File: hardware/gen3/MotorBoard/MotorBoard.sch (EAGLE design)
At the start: 265 parts, among them M10O1 TEST_PT, M1O2 TEST_PT, M1O3 TEST_PT, M2O1 TEST_PT, M2O2 TEST_PT, M2O3 TEST_PT, M3O1 TEST_PT, M3O2 TEST_PT, M3O3 TEST_PT, M4O1 TEST_PT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

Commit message: motorbrd: just felt like I should commit
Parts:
- added R113: 10k, SparkFun-Passives:RESISTOR0805-RES
- added S1: SWITCH-MOMENTARY-2SMD-4, SparkFun-Electromechanical:SWITCH-MOMENTARY-2SMD-4
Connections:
- new net RESET1: R113.1, S1.1
- net 3.3V: now also R113.2
- net GND: now also S1.2
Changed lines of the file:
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@@
 <?xml version="1.0" encoding="utf-8"?>
 <!DOCTYPE eagle SYSTEM "eagle.dtd">
-<eagle version="7.2.0">
+<eagle version="6.4">
 <drawing>
 <settings>
@@
 <part name="C57" library="SparkFun-Passives" deviceset="CAP" device="0805" value=".1uF"/>
 <part name="C58" library="SparkFun-Passives" deviceset="CAP" device="0805" value=".1uF"/>
+<part name="S1" library="SparkFun-Electromechanical" deviceset="SWITCH-MOMENTARY-2" device="SMD-4"/>
+<part name="R113" library="SparkFun-Passives" deviceset="RESISTOR" device="0805-RES" value="10k"/>
 </parts>
 <sheets>
@@
 <instance part="C57" gate="G$1" x="327.66" y="223.52"/>
 <instance part="C58" gate="G$1" x="393.7" y="220.98"/>
+<instance part="S1" gate="G$1" x="167.64" y="144.78"/>
+<instance part="R113" gate="G$1" x="170.18" y="132.08"/>
 </instances>
 <busses>
@@
 <label x="485.14" y="152.4" size="1.778" layer="95"/>
 </segment>
+<segment>
+<pinref part="S1" gate="G$1" pin="2"/>
+<wire x1="172.72" y1="144.78" x2="177.8" y2="144.78" width="0.1524" layer="91"/>
+<label x="175.26" y="144.78" size="1.778" layer="95"/>
+</segment>
 </net>
 <net name="3.3V" class="0">
@@
 <label x="469.9" y="165.1" size="1.778" layer="95"/>
 </segment>
+<segment>
+<pinref part="R113" gate="G$1" pin="2"/>
+<wire x1="175.26" y1="132.08" x2="177.8" y2="132.08" width="0.1524" layer="91"/>
+<label x="177.8" y="132.08" size="1.778" layer="95"/>
+</segment>
 </net>
 <net name="MOSI" class="0">
@@
 </segment>
 </net>
+<net name="RESET1" class="0">
+<segment>
+<wire x1="149.86" y1="132.08" x2="162.56" y2="132.08" width="0.1524" layer="91"/>
+<pinref part="S1" gate="G$1" pin="1"/>
+<wire x1="162.56" y1="132.08" x2="162.56" y2="144.78" width="0.1524" layer="91"/>
+<pinref part="R113" gate="G$1" pin="1"/>
+<wire x1="162.56" y1="132.08" x2="165.1" y2="132.08" width="0.1524" layer="91"/>
+<junction x="162.56" y="132.08"/>
+</segment>
+</net>

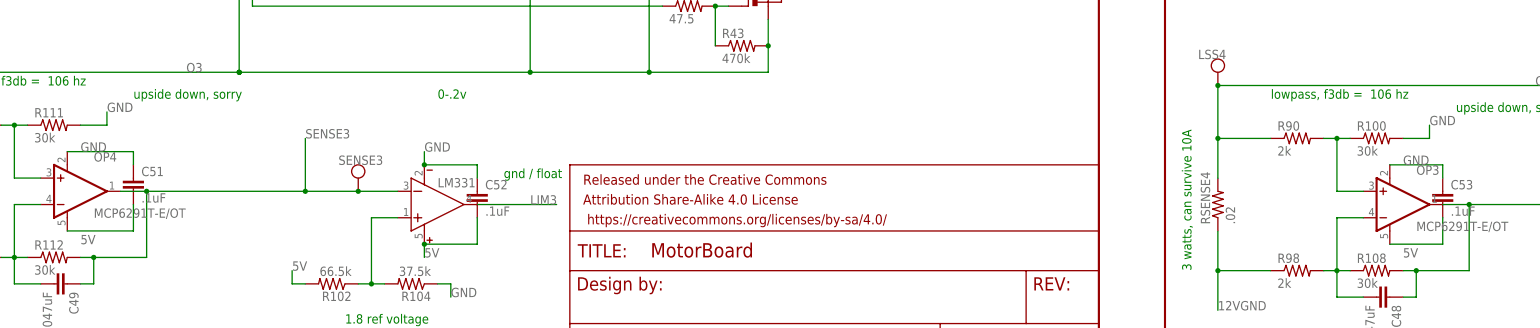
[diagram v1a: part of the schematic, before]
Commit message: fixed OP3 and OP4 mistake and cluttered inboxes
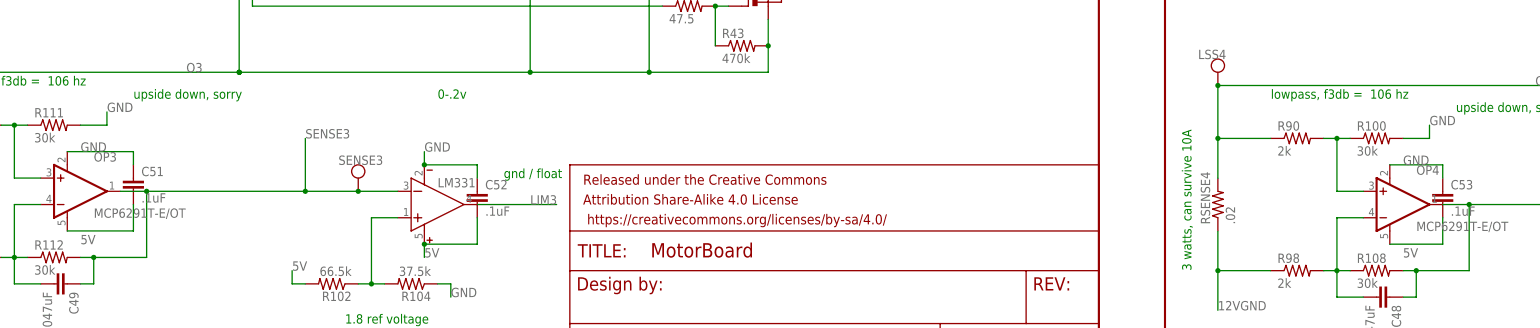
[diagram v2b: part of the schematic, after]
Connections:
- net N$67: now also OP4.+IN; no longer OP3.+IN
- net N$87: now also OP4.-IN; no longer OP3.-IN
- net N$89: now also OP3.+IN; no longer OP4.+IN
- net N$90: now also OP3.-IN; no longer OP4.-IN
- net SENSE3: now also OP3.OUT; no longer OP4.OUT
- net SENSE4: now also OP4.OUT; no longer OP3.OUT
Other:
- moved on the sheet: OP3, OP4
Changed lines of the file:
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@@
 <part name="R100" library="SparkFun-Passives" deviceset="RESISTOR" device="0805-RES" value="30k"/>
 <part name="R108" library="SparkFun-Passives" deviceset="RESISTOR" device="0805-RES" value="30k"/>
-<part name="OP3" library="SparkFun-AnalogIC" deviceset="MCP6291" device="T-E/OT"/>
+<part name="OP4" library="SparkFun-AnalogIC" deviceset="MCP6291" device="T-E/OT"/>
 <part name="RSENSE3" library="SparkFun-Resistors" deviceset="RESISTOR" device="2512" value=".02"/>
 <part name="R109" library="SparkFun-Passives" deviceset="RESISTOR" device="0805-RES" value="2k"/>
@@
 <part name="R111" library="SparkFun-Passives" deviceset="RESISTOR" device="0805-RES" value="30k"/>
 <part name="R112" library="SparkFun-Passives" deviceset="RESISTOR" device="0805-RES" value="30k"/>
-<part name="OP4" library="SparkFun-AnalogIC" deviceset="MCP6291" device="T-E/OT"/>
+<part name="OP3" library="SparkFun-AnalogIC" deviceset="MCP6291" device="T-E/OT"/>
 <part name="C47" library="SparkFun-Passives" deviceset="CAP" device="0805" value=".047uF"/>
 <part name="C1" library="SparkFun-Passives" deviceset="CAP" device="0805" value=".047uF"/>
@@
 <instance part="R100" gate="G$1" x="566.42" y="40.64"/>
 <instance part="R108" gate="G$1" x="566.42" y="15.24"/>
-<instance part="OP3" gate="G$1" x="568.96" y="27.94" rot="MR180"/>
+<instance part="OP4" gate="G$1" x="568.96" y="27.94" rot="MR180"/>
 <instance part="RSENSE3" gate="G$1" x="281.94" y="30.48" rot="R90"/>
 <instance part="R109" gate="G$1" x="297.18" y="43.18"/>
@@
 <instance part="R111" gate="G$1" x="312.42" y="43.18"/>
 <instance part="R112" gate="G$1" x="312.42" y="17.78"/>
-<instance part="OP4" gate="G$1" x="314.96" y="30.48" rot="MR180"/>
+<instance part="OP3" gate="G$1" x="314.96" y="30.48" rot="MR180"/>
 <instance part="C47" gate="G$1" x="312.42" y="208.28" rot="R270"/>
 <instance part="C1" gate="G$1" x="566.42" y="208.28" rot="R270"/>
@@
 <segment>
 <label x="571.5" y="35.56" size="1.778" layer="95"/>
-<pinref part="OP3" gate="G$1" pin="V-"/>
+<pinref part="OP4" gate="G$1" pin="V-"/>
 <pinref part="C53" gate="G$1" pin="1"/>
 <wire x1="568.96" y1="35.56" x2="579.12" y2="35.56" width="0.1524" layer="91"/>
@@
 <segment>
 <label x="317.5" y="38.1" size="1.778" layer="95"/>
-<pinref part="OP4" gate="G$1" pin="V-"/>
+<pinref part="OP3" gate="G$1" pin="V-"/>
 <pinref part="C51" gate="G$1" pin="1"/>
 <wire x1="314.96" y1="38.1" x2="327.66" y2="38.1" width="0.1524" layer="91"/>
@@
 <segment>
 <label x="571.5" y="17.78" size="1.778" layer="95"/>
-<pinref part="OP3" gate="G$1" pin="V+"/>
+<pinref part="OP4" gate="G$1" pin="V+"/>
 <pinref part="C53" gate="G$1" pin="2"/>
 <wire x1="568.96" y1="20.32" x2="579.12" y2="20.32" width="0.1524" layer="91"/>
@@
 <segment>
 <label x="317.5" y="20.32" size="1.778" layer="95"/>
-<pinref part="OP4" gate="G$1" pin="V+"/>
+<pinref part="OP3" gate="G$1" pin="V+"/>
 <pinref part="C51" gate="G$1" pin="2"/>
 <wire x1="327.66" y1="27.94" x2="327.66" y2="22.86" width="0.1524" layer="91"/>
@@
 <junction x="370.84" y="30.48"/>
 <wire x1="330.2" y1="30.48" x2="360.68" y2="30.48" width="0.1524" layer="91"/>
-<pinref part="OP4" gate="G$1" pin="OUT"/>
+<pinref part="OP3" gate="G$1" pin="OUT"/>
 <wire x1="325.12" y1="30.48" x2="330.2" y2="30.48" width="0.1524" layer="91"/>
 <pinref part="R112" gate="G$1" pin="2"/>
@@
 <segment>
 <wire x1="584.2" y1="27.94" x2="612.14" y2="27.94" width="0.1524" layer="91"/>
-<pinref part="OP3" gate="G$1" pin="OUT"/>
+<pinref part="OP4" gate="G$1" pin="OUT"/>
 <wire x1="579.12" y1="27.94" x2="584.2" y2="27.94" width="0.1524" layer="91"/>
 <pinref part="R108" gate="G$1" pin="2"/>
@@
 <wire x1="558.8" y1="40.64" x2="558.8" y2="30.48" width="0.1524" layer="91"/>
 <junction x="558.8" y="40.64"/>
-<pinref part="OP3" gate="G$1" pin="+IN"/>
+<pinref part="OP4" gate="G$1" pin="+IN"/>
 <wire x1="563.88" y1="30.48" x2="558.8" y2="30.48" width="0.1524" layer="91"/>
 </segment>
@@
 <wire x1="558.8" y1="15.24" x2="561.34" y2="15.24" width="0.1524" layer="91"/>
 <junction x="558.8" y="15.24"/>
-<pinref part="OP3" gate="G$1" pin="-IN"/>
+<pinref part="OP4" gate="G$1" pin="-IN"/>
 <wire x1="563.88" y1="25.4" x2="558.8" y2="25.4" width="0.1524" layer="91"/>
 <pinref part="C48" gate="G$1" pin="2"/>
@@
 <wire x1="304.8" y1="43.18" x2="304.8" y2="33.02" width="0.1524" layer="91"/>
 <junction x="304.8" y="43.18"/>
-<pinref part="OP4" gate="G$1" pin="+IN"/>
+<pinref part="OP3" gate="G$1" pin="+IN"/>
 <wire x1="309.88" y1="33.02" x2="304.8" y2="33.02" width="0.1524" layer="91"/>
 </segment>
@@
 <wire x1="304.8" y1="17.78" x2="307.34" y2="17.78" width="0.1524" layer="91"/>
 <junction x="304.8" y="17.78"/>
-<pinref part="OP4" gate="G$1" pin="-IN"/>
+<pinref part="OP3" gate="G$1" pin="-IN"/>
 <wire x1="309.88" y1="27.94" x2="304.8" y2="27.94" width="0.1524" layer="91"/>
 <pinref part="C49" gate="G$1" pin="2"/>

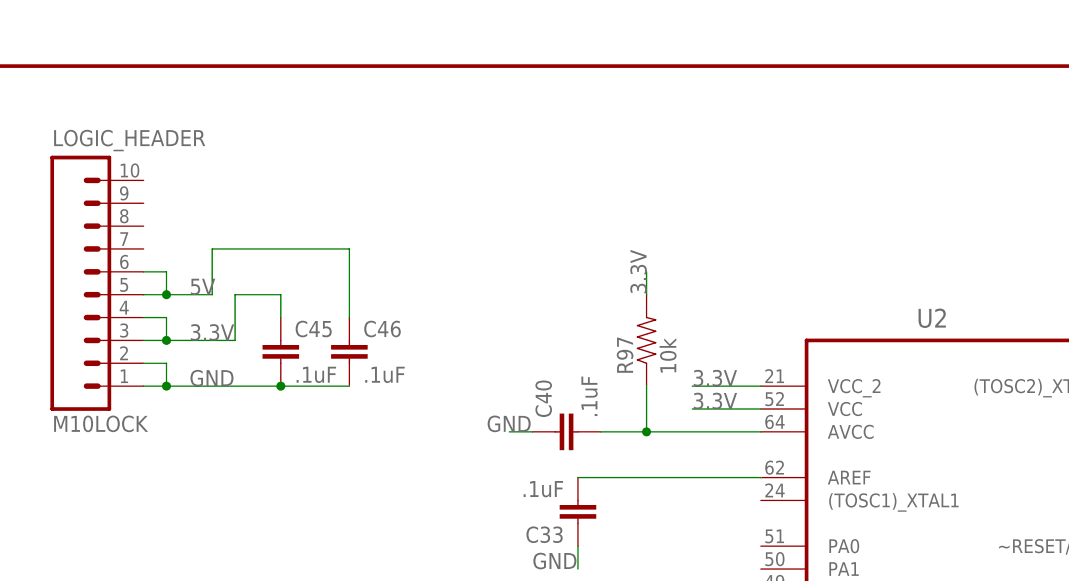
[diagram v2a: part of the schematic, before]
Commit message: added decoupling to motor
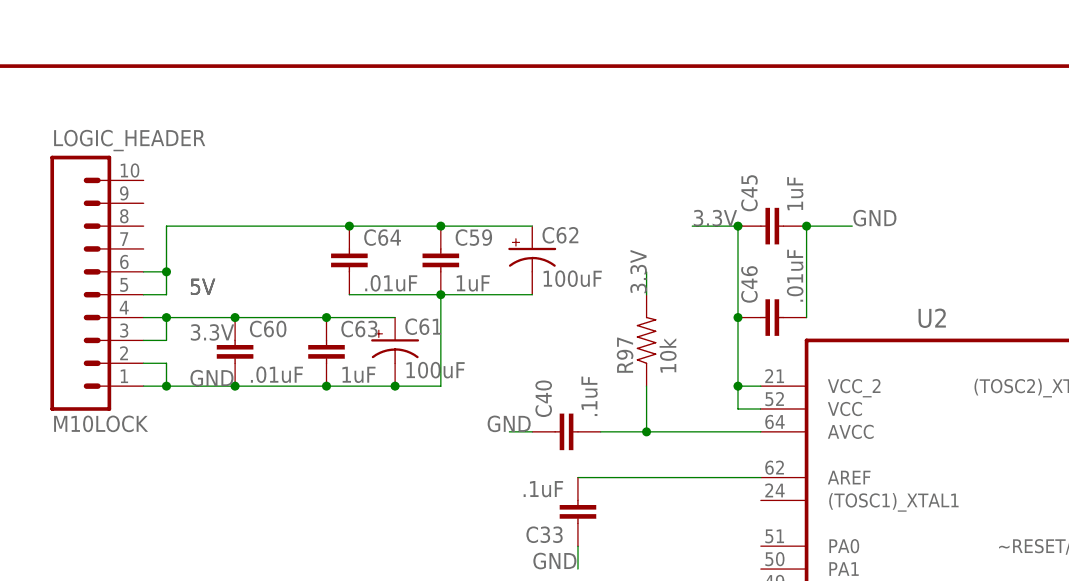
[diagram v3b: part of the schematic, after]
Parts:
- added C59, C63: 1uF, SparkFun-Capacitors:CAP0805
- added C60, C64: .01uF, SparkFun-Capacitors:CAP0805
- added C61, C62: 100uF, gen3:CAP-POLAR
- C45: value .1uF -> 1uF; device SparkFun-Passives:CAP0805 -> SparkFun-Capacitors:CAP0805
- C46: value .1uF -> .01uF; device SparkFun-Passives:CAP0805 -> SparkFun-Capacitors:CAP0805
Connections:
- net 3.3V: now also C46.1, C60.1, C61.+, C63.1
- net 5V: now also C59.1, C62.+, C64.1; no longer C46.1
- net GND: now also C59.2, C60.2, C61.-, C62.-, C63.2, C64.2
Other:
- moved on the sheet: C45, C46

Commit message: better fit caps for allegro
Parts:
- C10, C11, C18, C19, C20, C27, C28, C29, C36, C37, C38, C9: value .033uF -> .056uF
- C14, C23, C32, C5: value .68uF -> 1uF
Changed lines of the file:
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@@
 <part name="C4" library="SparkFun-Passives" deviceset="CAP" device="0805" value=".1uF"/>
 <part name="R5" library="SparkFun-Resistors" deviceset="RESISTOR" device="0805-RES" value="40.2k"/>
-<part name="C5" library="SparkFun-Passives" deviceset="CAP" device="0805" value=".68uF"/>
+<part name="C5" library="SparkFun-Passives" deviceset="CAP" device="0805" value="1uF"/>
 <part name="C6" library="SparkFun-Passives" deviceset="CAP" device="0805" value=".1uF"/>
 <part name="GND1" library="SparkFun-Aesthetics" deviceset="GND" device=""/>
@@
 <part name="R16" library="SparkFun-Resistors" deviceset="RESISTOR" device="0805-RES" value="470k"/>
 <part name="R17" library="SparkFun-Resistors" deviceset="RESISTOR" device="0805-RES" value="470k"/>
-<part name="C9" library="SparkFun-Passives" deviceset="CAP" device="0805" value=".033uF"/>
-<part name="C10" library="SparkFun-Passives" deviceset="CAP" device="0805" value=".033uF"/>
-<part name="C11" library="SparkFun-Passives" deviceset="CAP" device="0805" value=".033uF"/>
+<part name="C9" library="SparkFun-Passives" deviceset="CAP" device="0805" value=".056uF"/>
+<part name="C10" library="SparkFun-Passives" deviceset="CAP" device="0805" value=".056uF"/>
+<part name="C11" library="SparkFun-Passives" deviceset="CAP" device="0805" value=".056uF"/>
 <part name="RSENSE1" library="SparkFun-Resistors" deviceset="RESISTOR" device="2512" value=".02"/>
 <part name="Q9" library="rfc" deviceset="N-MOSFET" device=""/>
@@
 <part name="C13" library="SparkFun-Passives" deviceset="CAP" device="0805" value=".1uF"/>
 <part name="R18" library="SparkFun-Resistors" deviceset="RESISTOR" device="0805-RES" value="40.2k"/>
-<part name="C14" library="SparkFun-Passives" deviceset="CAP" device="0805" value=".68uF"/>
+<part name="C14" library="SparkFun-Passives" deviceset="CAP" device="0805" value="1uF"/>
 <part name="GND7" library="SparkFun-Aesthetics" deviceset="GND" device=""/>
 <part name="GND8" library="SparkFun-Aesthetics" deviceset="GND" device=""/>
@@
 <part name="R29" library="SparkFun-Resistors" deviceset="RESISTOR" device="0805-RES" value="470k"/>
 <part name="R30" library="SparkFun-Resistors" deviceset="RESISTOR" device="0805-RES" value="470k"/>
-<part name="C18" library="SparkFun-Passives" deviceset="CAP" device="0805" value=".033uF"/>
-<part name="C19" library="SparkFun-Passives" deviceset="CAP" device="0805" value=".033uF"/>
-<part name="C20" library="SparkFun-Passives" deviceset="CAP" device="0805" value=".033uF"/>
+<part name="C18" library="SparkFun-Passives" deviceset="CAP" device="0805" value=".056uF"/>
+<part name="C19" library="SparkFun-Passives" deviceset="CAP" device="0805" value=".056uF"/>
+<part name="C20" library="SparkFun-Passives" deviceset="CAP" device="0805" value=".056uF"/>
 <part name="Q17" library="rfc" deviceset="N-MOSFET" device=""/>
 <part name="U$2" library="rfc" deviceset="A4915" device=""/>
@@
 <part name="C22" library="SparkFun-Passives" deviceset="CAP" device="0805" value=".1uF"/>
 <part name="R31" library="SparkFun-Resistors" deviceset="RESISTOR" device="0805-RES" value="40.2k"/>
-<part name="C23" library="SparkFun-Passives" deviceset="CAP" device="0805" value=".68uF"/>
+<part name="C23" library="SparkFun-Passives" deviceset="CAP" device="0805" value="1uF"/>
 <part name="GND13" library="SparkFun-Aesthetics" deviceset="GND" device=""/>
 <part name="GND14" library="SparkFun-Aesthetics" deviceset="GND" device=""/>
@@
 <part name="R42" library="SparkFun-Resistors" deviceset="RESISTOR" device="0805-RES" value="470k"/>
 <part name="R43" library="SparkFun-Resistors" deviceset="RESISTOR" device="0805-RES" value="470k"/>
-<part name="C27" library="SparkFun-Passives" deviceset="CAP" device="0805" value=".033uF"/>
-<part name="C28" library="SparkFun-Passives" deviceset="CAP" device="0805" value=".033uF"/>
-<part name="C29" library="SparkFun-Passives" deviceset="CAP" device="0805" value=".033uF"/>
+<part name="C27" library="SparkFun-Passives" deviceset="CAP" device="0805" value=".056uF"/>
+<part name="C28" library="SparkFun-Passives" deviceset="CAP" device="0805" value=".056uF"/>
+<part name="C29" library="SparkFun-Passives" deviceset="CAP" device="0805" value=".056uF"/>
 <part name="Q25" library="rfc" deviceset="N-MOSFET" device=""/>
 <part name="U$3" library="rfc" deviceset="A4915" device=""/>
@@
 <part name="C31" library="SparkFun-Passives" deviceset="CAP" device="0805" value=".1uF"/>
 <part name="R44" library="SparkFun-Resistors" deviceset="RESISTOR" device="0805-RES" value="40.2k"/>
-<part name="C32" library="SparkFun-Passives" deviceset="CAP" device="0805" value=".68uF"/>
+<part name="C32" library="SparkFun-Passives" deviceset="CAP" device="0805" value="1uF"/>
 <part name="GND19" library="SparkFun-Aesthetics" deviceset="GND" device=""/>
 <part name="GND20" library="SparkFun-Aesthetics" deviceset="GND" device=""/>
@@
 <part name="R55" library="SparkFun-Resistors" deviceset="RESISTOR" device="0805-RES" value="470k"/>
 <part name="R56" library="SparkFun-Resistors" deviceset="RESISTOR" device="0805-RES" value="470k"/>
-<part name="C36" library="SparkFun-Passives" deviceset="CAP" device="0805" value=".033uF"/>
-<part name="C37" library="SparkFun-Passives" deviceset="CAP" device="0805" value=".033uF"/>
-<part name="C38" library="SparkFun-Passives" deviceset="CAP" device="0805" value=".033uF"/>
+<part name="C36" library="SparkFun-Passives" deviceset="CAP" device="0805" value=".056uF"/>
+<part name="C37" library="SparkFun-Passives" deviceset="CAP" device="0805" value=".056uF"/>
+<part name="C38" library="SparkFun-Passives" deviceset="CAP" device="0805" value=".056uF"/>
 <part name="R78" library="SparkFun-Resistors" deviceset="RESISTOR" device="0805-RES" value="1k"/>
 <part name="R79" library="SparkFun-Resistors" deviceset="RESISTOR" device="0805-RES" value="1k"/>

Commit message: DRC fixes for mtor
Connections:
- removed net RESET1: R113.1, S1.1
- net RESET: now also R113.1, S1.1
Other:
- moved on the sheet: C52, C53
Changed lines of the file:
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@@
 <instance part="C50" gate="G$1" x="419.1" y="162.56"/>
 <instance part="C51" gate="G$1" x="327.66" y="30.48"/>
-<instance part="C52" gate="G$1" x="393.7" y="27.94"/>
-<instance part="C53" gate="G$1" x="579.12" y="27.94"/>
+<instance part="C52" gate="G$1" x="396.24" y="27.94"/>
+<instance part="C53" gate="G$1" x="581.66" y="27.94"/>
 <instance part="C54" gate="G$1" x="647.7" y="25.4"/>
 <instance part="C55" gate="G$1" x="650.24" y="220.98"/>
@@
 <pinref part="COMP3" gate="G$1" pin="V-"/>
 <pinref part="C52" gate="G$1" pin="1"/>
-<wire x1="383.54" y1="35.56" x2="393.7" y2="35.56" width="0.1524" layer="91"/>
-<wire x1="393.7" y1="35.56" x2="393.7" y2="33.02" width="0.1524" layer="91"/>
+<wire x1="383.54" y1="35.56" x2="396.24" y2="35.56" width="0.1524" layer="91"/>
+<wire x1="396.24" y1="35.56" x2="396.24" y2="33.02" width="0.1524" layer="91"/>
 <junction x="383.54" y="35.56"/>
 </segment>
@@
 <pinref part="OP4" gate="G$1" pin="V-"/>
 <pinref part="C53" gate="G$1" pin="1"/>
-<wire x1="568.96" y1="35.56" x2="579.12" y2="35.56" width="0.1524" layer="91"/>
-<wire x1="579.12" y1="35.56" x2="579.12" y2="33.02" width="0.1524" layer="91"/>
+<wire x1="568.96" y1="35.56" x2="581.66" y2="35.56" width="0.1524" layer="91"/>
+<wire x1="581.66" y1="35.56" x2="581.66" y2="33.02" width="0.1524" layer="91"/>
 </segment>
 <segment>
@@
 <net name="RESET" class="0">
 <segment>
-<pinref part="U2" gate="A" pin="~RESET/PG5"/>
-<wire x1="144.78" y1="132.08" x2="152.4" y2="132.08" width="0.1524" layer="91"/>
-<label x="147.32" y="132.08" size="1.778" layer="95"/>
-</segment>
-<segment>
 <pinref part="JP1" gate="G$1" pin="5"/>
 <wire x1="71.12" y1="38.1" x2="66.04" y2="38.1" width="0.1524" layer="91"/>
 <label x="63.5" y="38.1" size="1.778" layer="95"/>
 </segment>
+<segment>
+<pinref part="S1" gate="G$1" pin="1"/>
+<wire x1="162.56" y1="132.08" x2="162.56" y2="144.78" width="0.1524" layer="91"/>
+<pinref part="R113" gate="G$1" pin="1"/>
+<wire x1="162.56" y1="132.08" x2="165.1" y2="132.08" width="0.1524" layer="91"/>
+<junction x="162.56" y="132.08"/>
+<pinref part="U2" gate="A" pin="~RESET/PG5"/>
+<wire x1="144.78" y1="132.08" x2="162.56" y2="132.08" width="0.1524" layer="91"/>
+<label x="147.32" y="132.08" size="1.778" layer="95"/>
+</segment>
 </net>
 <net name="12V" class="0">
@@
 <pinref part="COMP3" gate="G$1" pin="V+"/>
 <pinref part="C52" gate="G$1" pin="2"/>
-<wire x1="383.54" y1="20.32" x2="393.7" y2="20.32" width="0.1524" layer="91"/>
-<wire x1="393.7" y1="20.32" x2="393.7" y2="25.4" width="0.1524" layer="91"/>
+<wire x1="383.54" y1="20.32" x2="396.24" y2="20.32" width="0.1524" layer="91"/>
+<wire x1="396.24" y1="20.32" x2="396.24" y2="25.4" width="0.1524" layer="91"/>
 <junction x="383.54" y="20.32"/>
 </segment>
@@
 <pinref part="OP4" gate="G$1" pin="V+"/>
 <pinref part="C53" gate="G$1" pin="2"/>
-<wire x1="568.96" y1="20.32" x2="579.12" y2="20.32" width="0.1524" layer="91"/>
-<wire x1="579.12" y1="20.32" x2="579.12" y2="25.4" width="0.1524" layer="91"/>
+<wire x1="568.96" y1="20.32" x2="581.66" y2="20.32" width="0.1524" layer="91"/>
+<wire x1="581.66" y1="20.32" x2="581.66" y2="25.4" width="0.1524" layer="91"/>
 </segment>
 <segment>
@@
 </segment>
 </net>
-<net name="RESET1" class="0">
-<segment>
-<wire x1="149.86" y1="132.08" x2="162.56" y2="132.08" width="0.1524" layer="91"/>
-<pinref part="S1" gate="G$1" pin="1"/>
-<wire x1="162.56" y1="132.08" x2="162.56" y2="144.78" width="0.1524" layer="91"/>
-<pinref part="R113" gate="G$1" pin="1"/>
-<wire x1="162.56" y1="132.08" x2="165.1" y2="132.08" width="0.1524" layer="91"/>
-<junction x="162.56" y="132.08"/>
-</segment>
-</net>
